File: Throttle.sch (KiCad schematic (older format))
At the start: 5 parts

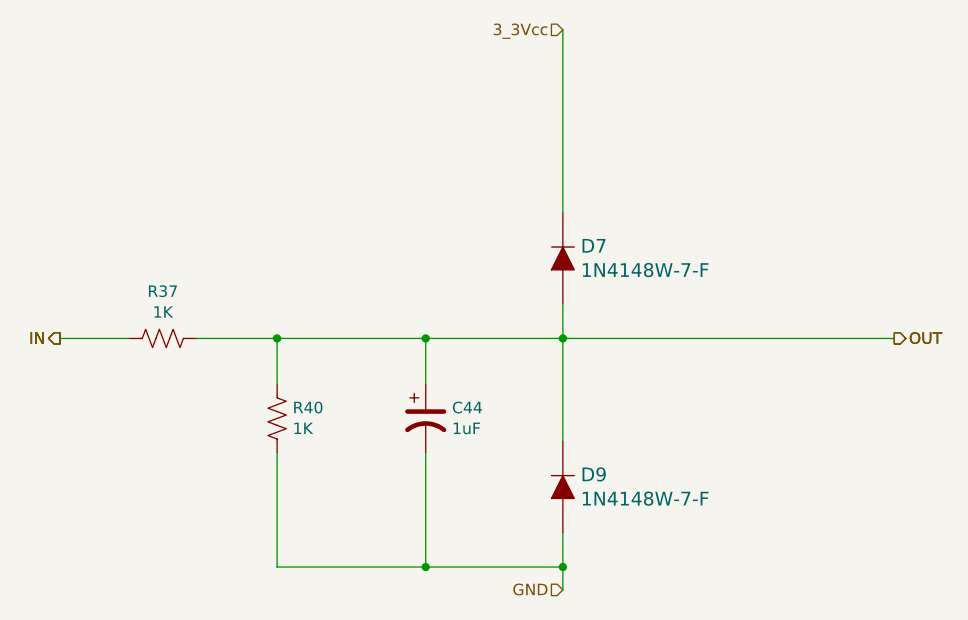
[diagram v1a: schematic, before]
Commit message: 4 layer board that passes checks
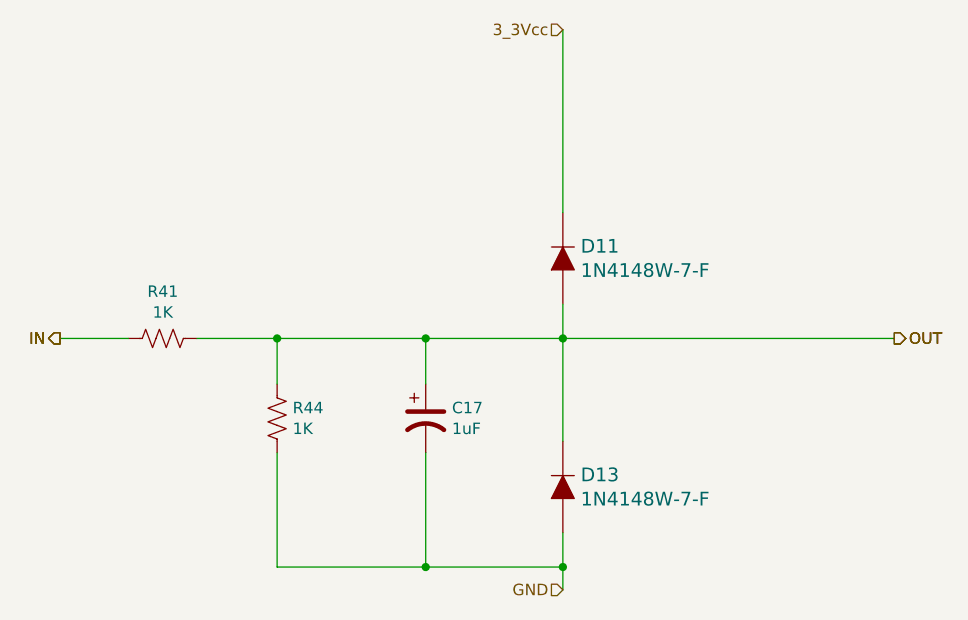
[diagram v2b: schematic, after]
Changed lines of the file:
@@
 $Descr A4 11693 8268
 encoding utf-8
-Sheet 13 37
+Sheet 13 36
 Title ""
 Date ""
@@
 AR Path="/60D76413/60493A95" Ref="C22"  Part="1"
 AR Path="/61336D3E/60493A95" Ref="C17"  Part="1"
-F 0 "C44" H 4865 3646 50  0000 L CNN
+F 0 "C17" H 4865 3646 50  0000 L CNN
 F 1 "1uF" H 4865 3555 50  0000 L CNN
 F 2 "Capacitor_SMD:C_0805_2012Metric" H 4750 3600 50  0001 C CNN
@@
 AR Path="/60D76413/60493A96" Ref="R46"  Part="1"
 AR Path="/61336D3E/60493A96" Ref="R44"  Part="1"
-F 0 "R40" H 4168 3646 50  0000 L CNN
+F 0 "R44" H 4168 3646 50  0000 L CNN
 F 1 "1K" H 4168 3555 50  0000 L CNN
 F 2 "Resistor_SMD:R_0805_2012Metric" V 4140 3590 50  0001 C CNN
@@
 AR Path="/60D76413/6048CB3B" Ref="D10"  Part="1"
 AR Path="/61336D3E/6048CB3B" Ref="D11"  Part="1"
-F 0 "D7" V 5403 2822 60  0000 R CNN
+F 0 "D11" V 5403 2822 60  0000 R CNN
 F 1 "1N4148W-7-F" V 5297 2822 60  0000 R CNN
 F 2 "digikey-footprints:SOD-123" H 5550 3100 60  0001 L CNN
@@
 AR Path="/60D76413/6048D3ED" Ref="D12"  Part="1"
 AR Path="/61336D3E/6048D3ED" Ref="D13"  Part="1"
-F 0 "D9" V 5403 3822 60  0000 R CNN
+F 0 "D13" V 5403 3822 60  0000 R CNN
 F 1 "1N4148W-7-F" V 5297 3822 60  0000 R CNN
 F 2 "digikey-footprints:SOD-123" H 5550 4100 60  0001 L CNN
@@
 AR Path="/60D76413/6048E020" Ref="R45"  Part="1"
 AR Path="/61336D3E/6048E020" Ref="R41"  Part="1"
-F 0 "R37" V 3395 3250 50  0000 C CNN
+F 0 "R41" V 3395 3250 50  0000 C CNN
 F 1 "1K" V 3486 3250 50  0000 C CNN
 F 2 "Resistor_SMD:R_0805_2012Metric" V 3640 3240 50  0001 C CNN

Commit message: Routed PCB
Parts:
- C44: JLCPCB_PN (none) -> C28323
- D7, D9: JLCPCB_PN (none) -> C81598
- R37, R40: JLCPCB_PN (none) -> C17513
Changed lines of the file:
@@
 F 2 "Capacitor_SMD:C_0805_2012Metric" H 4750 3600 50  0001 C CNN
 F 3 "~" H 4750 3600 50  0001 C CNN
+F 4 "C28323" H 4750 3600 50  0001 C CNN "JLCPCB_PN"
 	1    4750 3600
 	1    0    0    -1
@@
 F 2 "Resistor_SMD:R_0805_2012Metric" V 4140 3590 50  0001 C CNN
 F 3 "~" H 4100 3600 50  0001 C CNN
+F 4 "C17513" H 4100 3600 50  0001 C CNN "JLCPCB_PN"
 	1    4100 3600
 	1    0    0    -1
@@
 F 11 "Diodes Incorporated" H 5550 4000 60  0001 L CNN "Manufacturer"
 F 12 "Active" H 5550 4100 60  0001 L CNN "Status"
+F 13 "C81598" H 5350 2900 50  0001 C CNN "JLCPCB_PN"
 	1    5350 2900
 	0    -1   -1   0
@@
 F 11 "Diodes Incorporated" H 5550 5000 60  0001 L CNN "Manufacturer"
 F 12 "Active" H 5550 5100 60  0001 L CNN "Status"
+F 13 "C81598" H 5350 3900 50  0001 C CNN "JLCPCB_PN"
 	1    5350 3900
 	0    -1   -1   0
@@
 F 2 "Resistor_SMD:R_0805_2012Metric" V 3640 3240 50  0001 C CNN
 F 3 "~" H 3600 3250 50  0001 C CNN
+F 4 "C17513" H 3600 3250 50  0001 C CNN "JLCPCB_PN"
 	1    3600 3250
 	0    1    1    0
